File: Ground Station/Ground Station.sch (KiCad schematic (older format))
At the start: 1 part, among them IC1 ADP3335

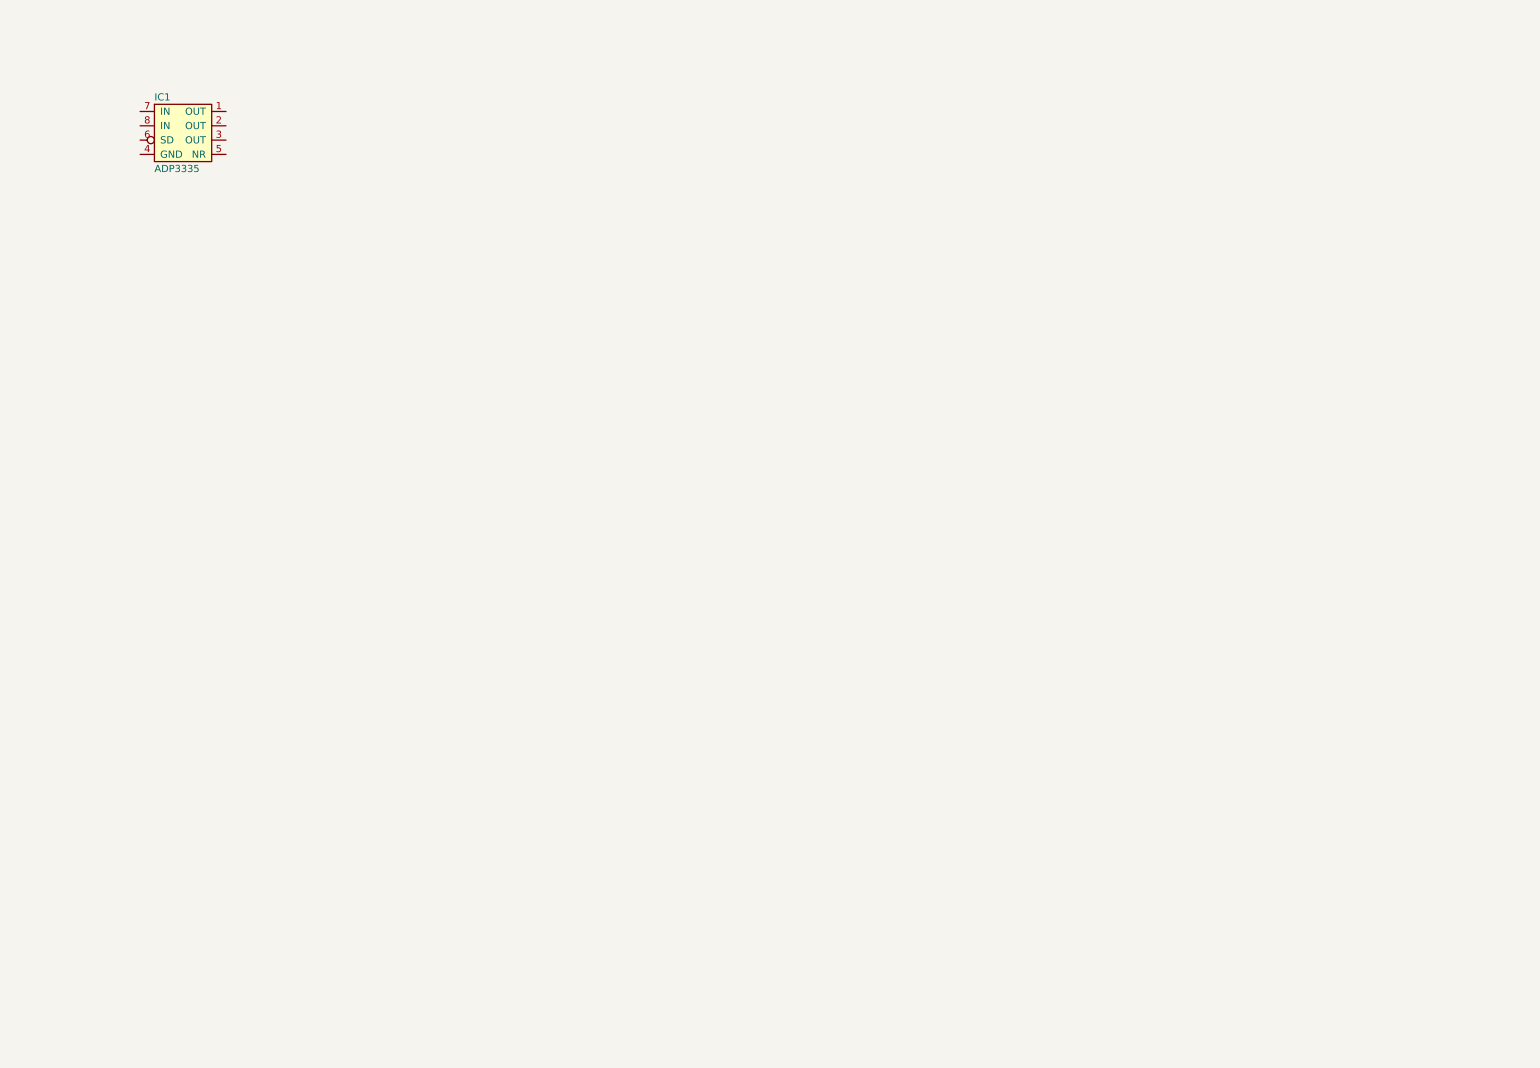
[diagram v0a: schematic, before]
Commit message: Finished Ground Station Schemnatic
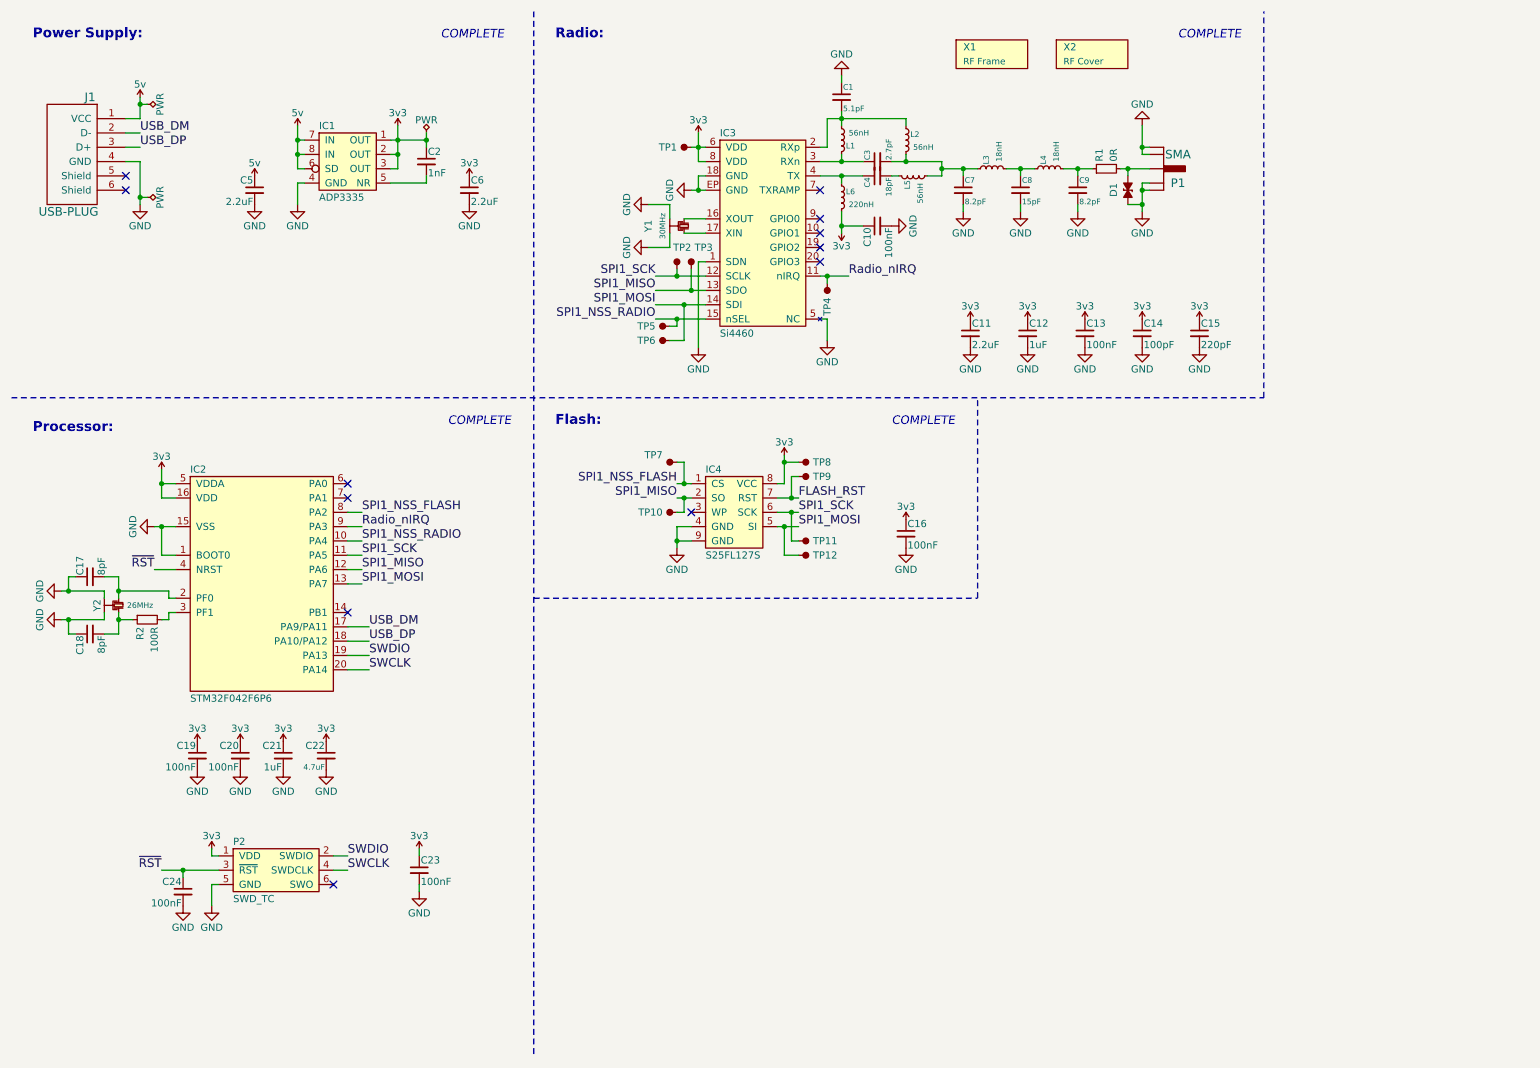
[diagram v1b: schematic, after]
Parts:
- added C1: 5.1pF, agg:0402-L, symbol C_Small
- added C10, C13, C16, C19, C20, C23, C24: 100nF, agg:0402-L, symbol C_Small
- added C11, C5, C6: 2.2uF, agg:0603-L, symbol C_Small
- added C12: 1uF, agg:0603-L, symbol C_Small
- added C14: 100pF, agg:0402-L, symbol C_Small
- added C15: 220pF, agg:0402-L, symbol C_Small
- added C17, C18: 8pF, agg:0402-L, symbol C_Small
- added C2: 1nF, agg:0402-L, symbol C_Small
- added C21: 1uF, agg:0402-L, symbol C_Small
- added C22: 4.7uF, agg:0402-L, symbol C_Small
- added C3: 2.7pF, agg:0402-L, symbol C_Small
- added C4: 18pF, agg:0402-L, symbol C_Small
- added C7, C9: 8.2pF, agg:0402-L, symbol C_Small
- added C8: 15pF, agg:0402-L, symbol C_Small
- added D1: ESD_DIODE, agg:0402-L, symbol ESD_DIODE
- added IC2: STM32F042F6P6, agg:TSSOP20, symbol STM32F042F6P6
- added IC3: Si4460, agg:QFN-20-EP-SI, symbol Si4460
- added IC4: S25FL127S, agg:WND008, symbol S25FL127S
- added J1: USB-PLUG, agg:MOLEX 48037-0001, symbol USB-PLUG
- added L1, L2, L5: 56nH, agg:0402-L, symbol L_Small
- added L3, L4: 18nH, agg:0402-L, symbol L_Small
- added L6: 220nH, agg:0603-L, symbol L_Small
- added P1: SMA, Library:SMA-J-P-H-ST-EM1, symbol SMA
- added P2: SWD_TC, agg:TC2030-NL, symbol SWD_TC
- added R1: 0R, agg:0402-L, symbol R_Small
- added R2: 100R, agg:0402-L, symbol R_Small
- added TP1, TP10, TP11, TP12, TP2, TP3, TP4, TP5, TP6, TP7, TP8, TP9: TESTPAD, agg:TESTPAD, symbol TESTPAD
- added X1: RF Frame, Library:BMI-S-201-F, symbol PART
- added X2: RF Cover, symbol PART
- added Y1: 30MHz, agg:XTAL-20x16, symbol SMD_XTAL
- added Y2: 26MHz, agg:XTAL-20x16, symbol SMD_XTAL
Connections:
- net 3v3: now reaches IC1.1 (OUT)
- net 3v3: now also IC1.2 (OUT), IC1.3 (OUT), C10.1, C11.1, C12.1, C13.1, C14.1, C15.1, C16.1, C19.1, C2.1, C20.1, C21.1, C22.1, C23.1, C6.1, IC2.16 (VDD), IC2.5 (VDDA), IC3.6 (VDD), IC3.8 (VDD), IC4.8 (VCC), L6.2, P2.1 (VDD), TP1.1 (TP), TP8.1 (TP)
- net GND: now reaches IC1.4 (GND)
- net GND: now also C1.1, C10.2, C11.2, C12.2, C13.2, C14.2, C15.2, C16.2, C17.1, C18.1, C19.2, C20.2, C21.2, C22.2, C23.2, C24.2, C5.2, C6.2, C7.2, C8.2, C9.2, D1.2, IC2.1 (BOOT0), IC2.15 (VSS), IC3.1 (SDN), IC3.18 (GND), IC3.5 (NC), IC3.EP (GND), IC4.4 (GND), IC4.9 (GND), J1.4 (GND), P1.2 (GND), P1.3 (GND), P1.4 (GND), P1.5 (GND), P2.5 (GND), Y1.2, Y1.4, Y2.2, Y2.4
- net at IC1.5 (NR): now also C2.2
- net 5v: now reaches IC1.6 (SD)
- net 5v: now also IC1.7 (IN), IC1.8 (IN), C5.1, J1.1 (VCC)
- new net: C17.2, IC2.2 (PF0), Y2.1
- new net: IC2.3 (PF1), R2.2
- new net: D1.1, P1.1 (RF), R1.2
- new net: IC3.16 (XOUT), Y1.1
- new net: IC3.17 (XIN), Y1.3
- new net: C1.2, IC3.2 (RXp), L1.2, L2.1
- new net: C3.1, IC3.3 (RXn), L1.1
- new net: C4.1, IC3.4 (TX), L6.1
- new net: C8.1, L3.2, L4.1
- new net: C3.2, C7.1, L2.2, L3.1, L5.2
- new net: C4.2, L5.1
- new net: C9.1, L4.2, R1.1
- new net: C18.2, R2.1, Y2.3
- new net FLASH_RST: IC4.7 (RST), TP9.1 (TP)
- new net Radio_nIRQ: IC2.9 (PA3), IC3.11 (nIRQ), TP4.1 (TP)
- new net SPI1_MISO: IC2.12 (PA6), IC3.13 (SDO), IC4.2 (SO), TP10.1 (TP), TP3.1 (TP)
- new net SPI1_MOSI: IC2.13 (PA7), IC3.14 (SDI), IC4.5 (SI), TP12.1 (TP), TP6.1 (TP)
- new net SPI1_NSS_FLASH: IC2.8 (PA2), IC4.1 (CS), TP7.1 (TP)
- new net SPI1_NSS_RADIO: IC2.10 (PA4), IC3.15 (nSEL), TP5.1 (TP)
- new net SPI1_SCK: IC2.11 (PA5), IC3.12 (SCLK), IC4.6 (SCK), TP11.1 (TP), TP2.1 (TP)
- new net SWCLK: IC2.20 (PA14), P2.4 (SWDCLK)
- new net SWDIO: IC2.19 (PA13), P2.2 (SWDIO)
- new net USB_DM: IC2.17 (PA9/PA11), J1.2 (D-)
- new net USB_DP: IC2.18 (PA10/PA12), J1.3 (D+)
- new net ~RST: C24.1, IC2.4 (NRST), P2.3 (~RST)
- no-connect marks 0 -> 12
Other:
- note added: "COMPLETE"
- note added: "Flash:"
- note added: "Power Supply:"
- note added: "Processor:"
- note added: "Radio:"
- moved on the sheet: IC1

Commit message: Finished ground station
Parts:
- added D2, D3: LED, agg:0603-LED, symbol LED
- added R3, R4: 1k, agg:0402-L, symbol R_Small
- added X3: Casing, symbol PART
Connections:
- net FLASH_RST: now also IC2.14 (PB1)
- net GND: now also D2.1 (K), D3.1 (K)
- net STAT_HBT: now reaches IC2.6 (PA0)
- net STAT_HBT: now also R3.1
- net STAT_WRN: now reaches IC2.7 (PA1)
- net STAT_WRN: now also R4.1
- new net: D3.2 (A), R4.2
- new net: D2.2 (A), R3.2
- no-connect marks 12 -> 9
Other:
- note added: "Status:"
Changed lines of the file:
@@
 	4150 500  4150 7800
 Wire Notes Line
-	9250 3200 9250 500
+	9250 4600 9250 500
 Wire Wire Line
 	850  4550 1150 4550
@@
 Wire Wire Line
 	2850 4500 2950 4500
-NoConn ~ 2850 3800
-NoConn ~ 2850 3900
-NoConn ~ 2850 4700
 Wire Wire Line
 	2850 4100 2950 4100
@@
 $EndComp
 Wire Wire Line
-	1300 1250 1400 1250
-Wire Wire Line
-	1400 1250 1400 1100
+	1400 1250 1300 1250
+Wire Wire Line
+	1400 1100 1400 1250
 $Comp
 L 5v #PWR043
@@
 Connection ~ 2500 1400
 Wire Wire Line
-	3150 1600 3200 1600
-Wire Wire Line
-	3200 1600 3200 1300
+	3200 1600 3150 1600
+Wire Wire Line
+	3200 1300 3200 1600
 Wire Wire Line
 	3150 1400 3400 1400
@@
 Flash:
 Wire Notes Line
-	4150 4600 7250 4600
+	4150 4600 9250 4600
 Wire Notes Line
 	7250 4600 7250 3200
@@
 Text Notes 6650 3400 0    60   Italic 0
 COMPLETE
+$Comp
+L PART X3
+U 1 1 571A249D
+P 10600 6950
+F 0 "X3" H 10650 7050 50  0000 L CNN
+F 1 "Casing" H 10650 6950 45  0000 L CNN
+F 2 "" H 10600 6950 50  0001 C CNN
+F 3 "http://www.farnell.com/datasheets/24163.pdf" H 10600 6950 50  0001 C CNN
+F 4 "1210437" H 10600 6950 60  0001 C CNN "Farnell"
+	1    10600 6950
+	1    0    0    -1
+$EndComp
+$Comp
+L LED D3
+U 1 1 571C20A4
+P 8550 4100
+F 0 "D3" H 8550 4200 50  0000 C CNN
+F 1 "LED" H 8550 4000 50  0000 C CNN
+F 2 "agg:0603-LED" H 8550 4100 50  0001 C CNN
+F 3 "http://www.farnell.com/datasheets/302470.pdf" H 8550 4100 50  0001 C CNN
+F 4 "1226390" H 8550 4100 60  0001 C CNN "Farnell"
+	1    8550 4100
+	0    -1   -1   0
+$EndComp
+$Comp
+L GND #PWR058
+U 1 1 571C20AB
+P 7750 4300
+F 0 "#PWR058" H 7750 4050 50  0001 C CNN
+F 1 "GND" H 7750 4150 50  0000 C CNN
+F 2 "" H 7750 4300 50  0000 C CNN
+F 3 "" H 7750 4300 50  0000 C CNN
+	1    7750 4300
+	1    0    0    -1
+$EndComp
+$Comp
+L GND #PWR059
+U 1 1 571C20B1
+P 8550 4300
+F 0 "#PWR059" H 8550 4050 50  0001 C CNN
+F 1 "GND" H 8550 4150 50  0000 C CNN
+F 2 "" H 8550 4300 50  0000 C CNN
+F 3 "" H 8550 4300 50  0000 C CNN
+	1    8550 4300
+	1    0    0    -1
+$EndComp
+Text Label 7800 3650 0    60   ~ 0
+STAT_HBT
+Text Label 8600 3650 0    60   ~ 0
+STAT_WRN
+$Comp
+L LED D2
+U 1 1 571C20BA
+P 7750 4100
+F 0 "D2" H 7750 4200 50  0000 C CNN
+F 1 "LED" H 7750 4000 50  0000 C CNN
+F 2 "agg:0603-LED" H 7750 4100 50  0001 C CNN
+F 3 "http://www.farnell.com/datasheets/1693302.pdf" H 7750 4100 50  0001 C CNN
+F 4 "1226372" H 7750 4100 60  0001 C CNN "Farnell"
+	1    7750 4100
+	0    -1   -1   0
+$EndComp
+$Comp
+L R_Small R3
+U 1 1 571C20C2
+P 7750 3800
+F 0 "R3" H 7800 3850 50  0000 L CNN
+F 1 "1k" H 7800 3750 50  0000 L CNN
+F 2 "agg:0402-L" H 7750 3800 50  0001 C CNN
+F 3 "http://www.farnell.com/datasheets/1716705.pdf" H 7750 3800 50  0001 C CNN
+F 4 "2072516" H 7750 3800 60  0001 C CNN "Farnell"
+	1    7750 3800
+	1    0    0    -1
+$EndComp
+$Comp
+L R_Small R4
+U 1 1 571C20CA
+P 8550 3800
+F 0 "R4" H 8600 3850 50  0000 L CNN
+F 1 "1k" H 8600 3750 50  0000 L CNN
+F 2 "agg:0402-L" H 8550 3800 50  0001 C CNN
+F 3 "http://www.farnell.com/datasheets/1716705.pdf" H 8550 3800 50  0001 C CNN
+F 4 "2072516" H 8550 3800 60  0001 C CNN "Farnell"
+	1    8550 3800
+	1    0    0    -1
+$EndComp
+Wire Wire Line
+	7750 3700 7750 3650
+Wire Wire Line
+	7750 3650 7800 3650
+Wire Wire Line
+	8550 3700 8550 3650
+Wire Wire Line
+	8550 3650 8600 3650
+Text Label 2950 3800 0    60   ~ 0
+STAT_HBT
+Text Label 2950 3900 0    60   ~ 0
+STAT_WRN
+Wire Wire Line
+	2850 3800 2950 3800
+Wire Wire Line
+	2950 3900 2850 3900
+Text Notes 7400 3400 0    69   ~ 14
+Status:
+Text Notes 8700 3400 0    60   Italic 0
+COMPLETE
+Text Label 3000 4700 0    60   ~ 0
+FLASH_RST
+Wire Wire Line
+	3000 4700 2850 4700
 $EndSCHEMATC

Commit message: Checked all Footprints
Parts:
- C8: Farnell 1973025 -> 2496795
- D2: Farnell 1226372 -> 1328306
- D3: Farnell 1226390 -> 1328309
- IC4: footprint agg:WND008 -> agg:S25FL127S
- R2: Farnell 1358015 -> 2072515
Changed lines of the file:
@@
 F 2 "agg:0402-L" H 7550 1750 50  0001 C CNN
 F 3 "http://www.farnell.com/datasheets/1446011.pdf" H 7550 1750 50  0001 C CNN
-F 4 "1973025" H 7550 1750 60  0001 C CNN "Farnell"
+F 4 "2496795" H 7550 1750 60  0001 C CNN "Farnell"
 	1    7550 1750
 	1    0    0    -1
@@
 F 2 "agg:0402-L" H 1450 4750 50  0001 C CNN
 F 3 "http://www.farnell.com/datasheets/1729045.pdf" H 1450 4750 50  0001 C CNN
-F 4 "1358015" H 1450 4750 60  0001 C CNN "Farnell"
+F 4 "2072515" H 1450 4750 60  0001 C CNN "Farnell"
 	1    1450 4750
 	0    -1   1    0
@@
 F 0 "IC4" H 5350 4300 50  0000 L CNN
 F 1 "S25FL127S" H 5350 3700 50  0000 L CNN
-F 2 "agg:WND008" H 5350 3600 50  0001 L CNN
+F 2 "agg:S25FL127S" H 5350 3600 50  0001 L CNN
 F 3 "https://www.spansion.com/Support/Datasheets/S25FL127S_00.pdf" H 5350 3500 50  0001 L CNN
 F 4 "2328003" H 5350 3400 50  0001 L CNN "Farnell"
@@
 F 2 "agg:0603-LED" H 8550 4100 50  0001 C CNN
 F 3 "http://www.farnell.com/datasheets/302470.pdf" H 8550 4100 50  0001 C CNN
-F 4 "1226390" H 8550 4100 60  0001 C CNN "Farnell"
+F 4 "1328309" H 8550 4100 60  0001 C CNN "Farnell"
 	1    8550 4100
 	0    -1   -1   0
@@
 F 2 "agg:0603-LED" H 7750 4100 50  0001 C CNN
 F 3 "http://www.farnell.com/datasheets/1693302.pdf" H 7750 4100 50  0001 C CNN
-F 4 "1226372" H 7750 4100 60  0001 C CNN "Farnell"
+F 4 "1328306" H 7750 4100 60  0001 C CNN "Farnell"
 	1    7750 4100
 	0    -1   -1   0

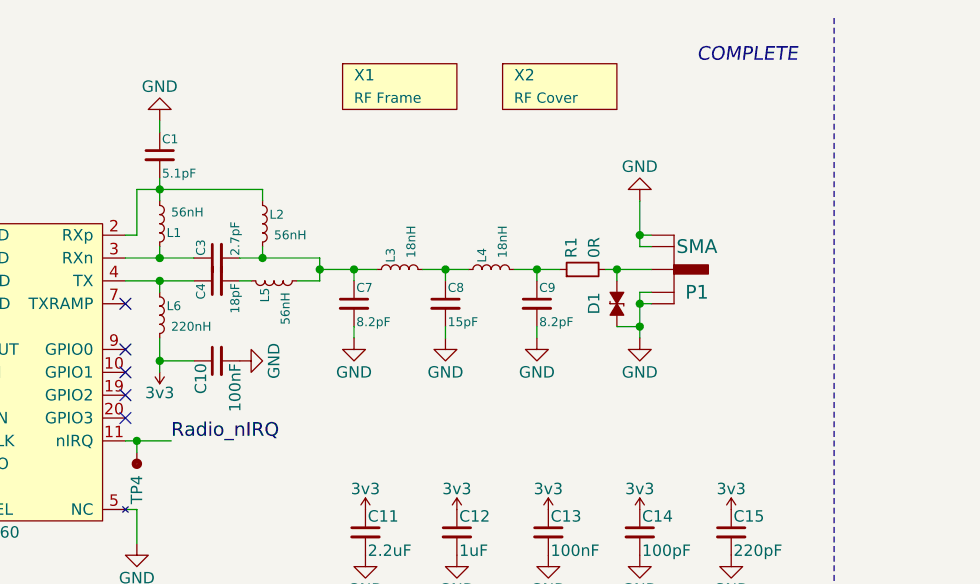
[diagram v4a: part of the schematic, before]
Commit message: Modified radio circuit to 868MHz and generated stickerBOM
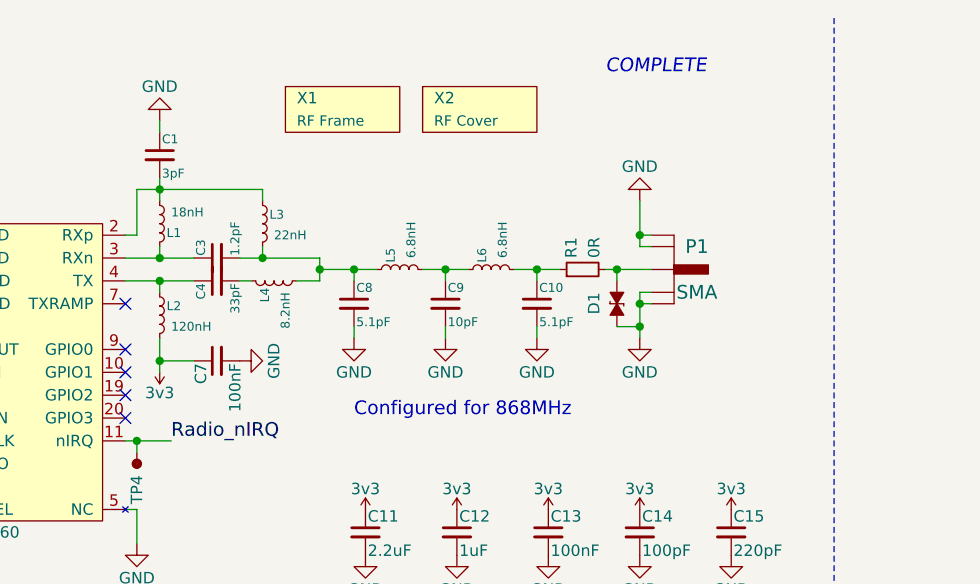
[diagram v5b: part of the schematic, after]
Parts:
- C1: value 5.1pF -> 3pF; Farnell 1885321 -> 2210752
- C10: value 100nF -> 5.1pF; Farnell 1828860 -> 1885321
- C3: value 2.7pF -> 1.2pF; Farnell 2310308 -> 2218843
- C4: value 18pF -> 33pF; Farnell 1885342 -> 2434643
- C7: value 8.2pF -> 100nF; Farnell 2310320 -> 1828860
- C8: value 15pF -> 5.1pF; Farnell 2496795 -> 1885321
- C9: value 8.2pF -> 10pF; Farnell 2310320 -> 1758941
- L1: value 56nH -> 18nH; Farnell 1669639 -> 1865775
- L2: value 56nH -> 120nH; footprint agg:0402-L -> agg:0603-L; Farnell 1669639 -> 2424731
- L3: value 18nH -> 22nH; Farnell 1760988 -> 1669580
- L4: value 18nH -> 8.2nH; Farnell 1760988 -> 1865771
- L5: value 56nH -> 6.8nH; Farnell 1669639 -> 1711736
- L6: value 220nH -> 6.8nH; footprint agg:0603-L -> agg:0402-L; Farnell 2215631 -> 1711736
- P1: footprint Library:SMA-J-P-H-ST-EM1 -> Library:SMA-142-0701-801; Farnell (none) -> 1019325; Samtec SMA-J-P-H-ST-EM1 -> (none)
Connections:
- net 3v3: now also C7.1, L2.2; no longer C10.1, L6.2
- net at C1.2, IC3.2 (RXp), L1.2: now also L3.1; no longer L2.1
- net at C4.1, IC3.4 (TX): now also L2.1; no longer L6.1
- net at C8.1, L3.2: now also C3.2, L4.2, L5.1; no longer L4.1
- net at C4.2: now also L4.1; no longer L5.1
- new net: C9.1, L5.2, L6.1
- new net: C10.1, L6.2, R1.1
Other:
- note added: "Configured for 868MHz"
